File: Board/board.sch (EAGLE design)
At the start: 51 parts, among them IC1 L297, IC2 MEGA32-P, IC3 L298, J1 +12V, Q1 BC639, Q3 BC639, U2 DS1621+, X1 WATER_PUMP, X2 FAN, X5 SM_CD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

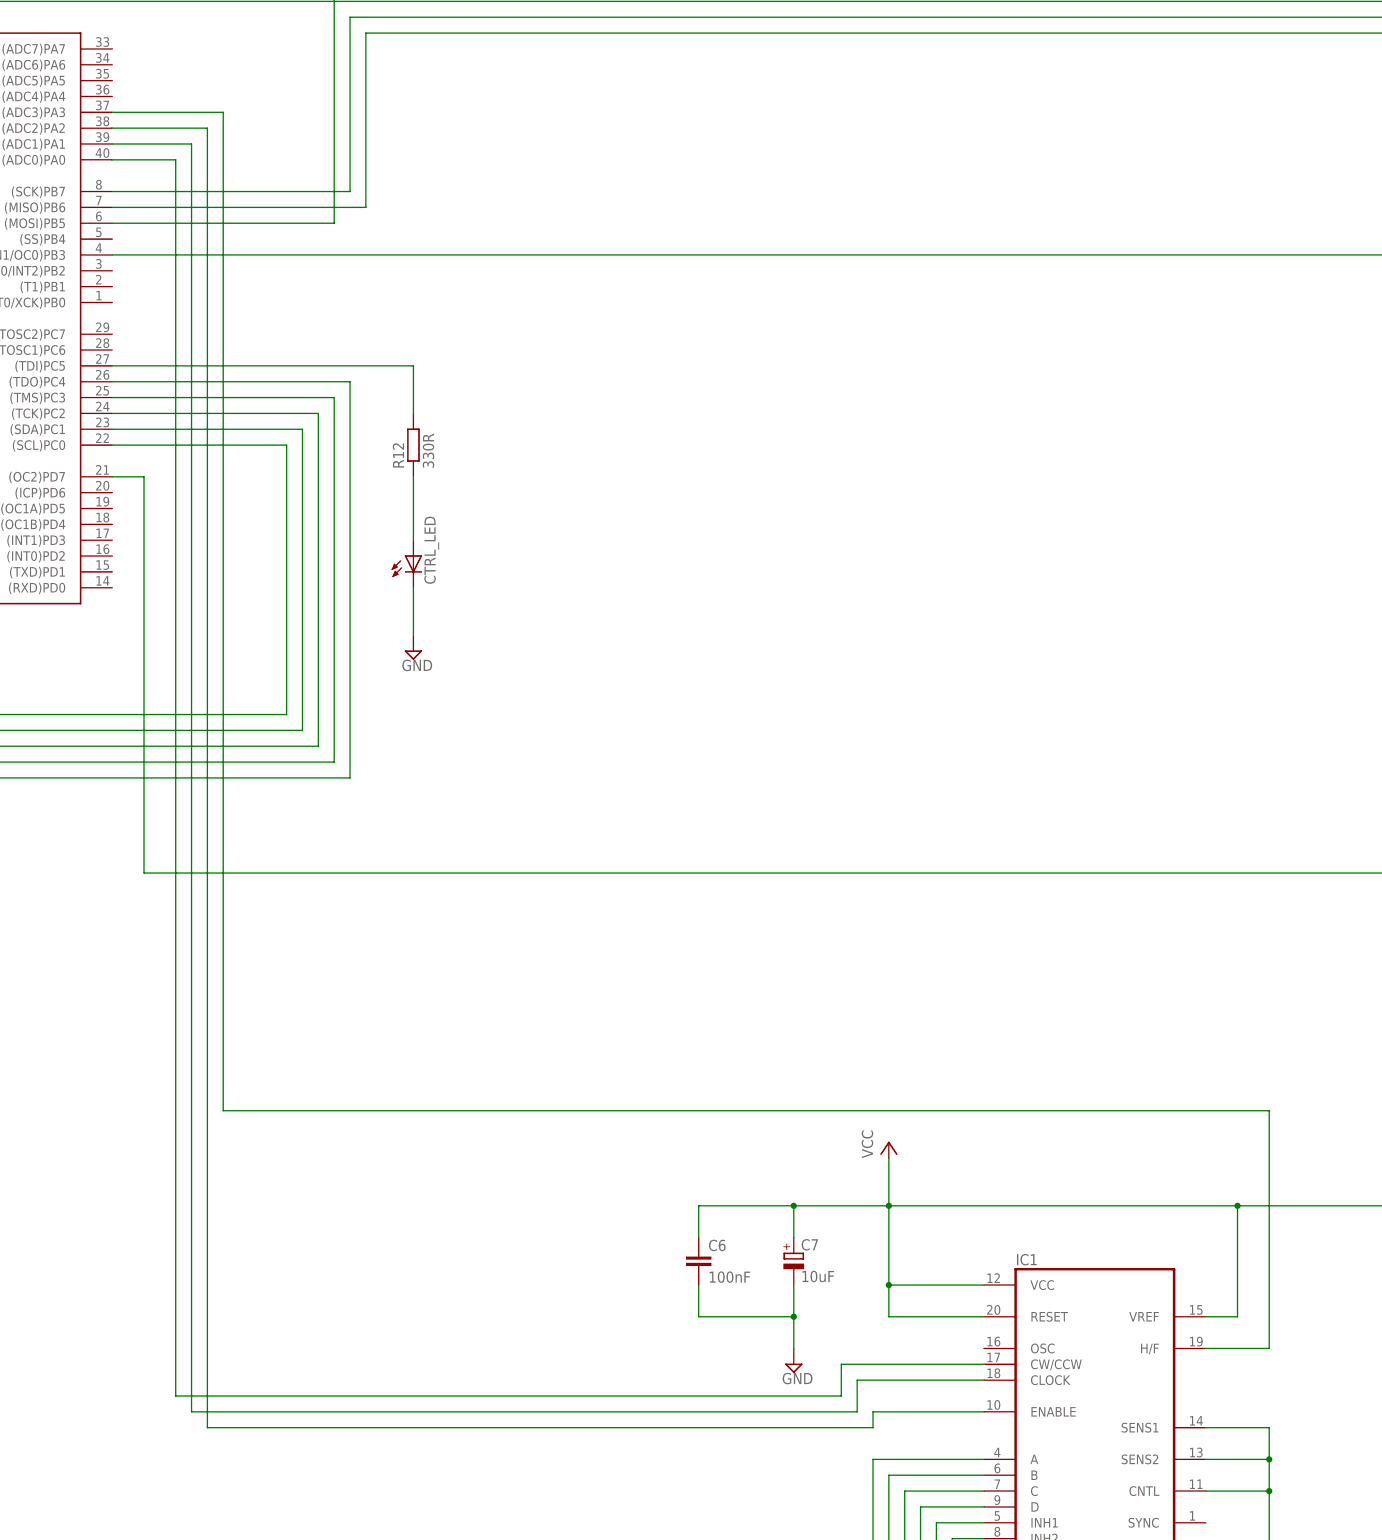
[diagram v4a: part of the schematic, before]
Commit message: PWM devices code
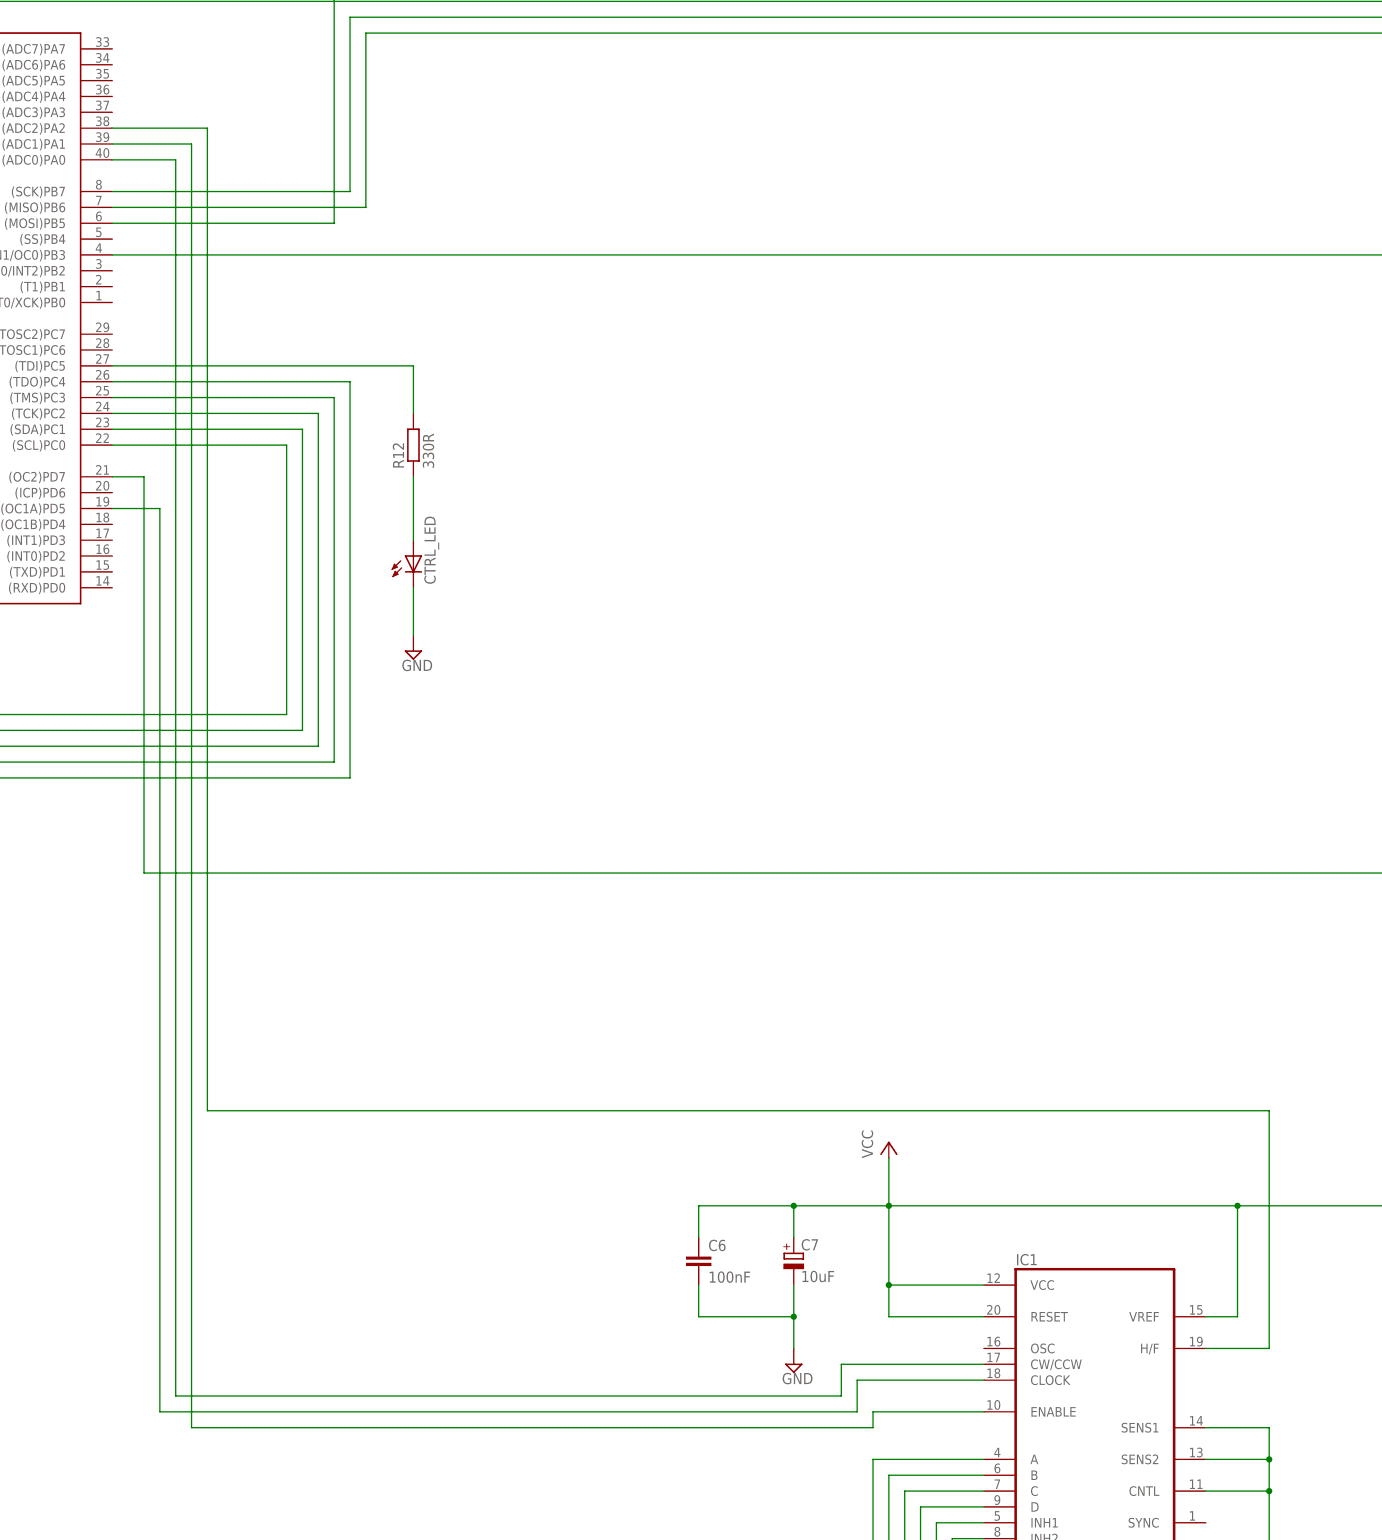
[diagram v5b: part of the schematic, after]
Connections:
- net N$18: now also IC2.(OC1A)PD5; no longer IC2.(ADC1)PA1
- net N$19: now also IC2.(ADC1)PA1; no longer IC2.(ADC2)PA2
- net N$20: now also IC2.(ADC2)PA2; no longer IC2.(ADC3)PA3
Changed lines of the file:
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@@
 <?xml version="1.0" encoding="utf-8"?>
 <!DOCTYPE eagle SYSTEM "eagle.dtd">
-<eagle version="7.6.0">
+<eagle version="8.7.1">
 <drawing>
 <settings>
 <setting alwaysvectorfont="no"/>
+<setting keepoldvectorfont="yes"/>
 <setting verticaltext="up"/>
 </settings>
@@
 <net name="N$18" class="0">
 <segment>
-<pinref part="IC2" gate="G$1" pin="(ADC1)PA1"/>
-<wire x1="-35.56" y1="38.1" x2="-22.86" y2="38.1" width="0.1524" layer="91"/>
-<wire x1="-22.86" y1="38.1" x2="-22.86" y2="-165.1" width="0.1524" layer="91"/>
-<wire x1="-22.86" y1="-165.1" x2="83.82" y2="-165.1" width="0.1524" layer="91"/>
+<wire x1="-27.94" y1="-165.1" x2="83.82" y2="-165.1" width="0.1524" layer="91"/>
 <pinref part="IC1" gate="L297" pin="CLOCK"/>
 <wire x1="104.14" y1="-160.02" x2="83.82" y2="-160.02" width="0.1524" layer="91"/>
 <wire x1="83.82" y1="-160.02" x2="83.82" y2="-165.1" width="0.1524" layer="91"/>
+<wire x1="-27.94" y1="-165.1" x2="-27.94" y2="-20.32" width="0.1524" layer="91"/>
+<pinref part="IC2" gate="G$1" pin="(OC1A)PD5"/>
+<wire x1="-27.94" y1="-20.32" x2="-35.56" y2="-20.32" width="0.1524" layer="91"/>
 </segment>
 </net>
 <net name="N$19" class="0">
 <segment>
-<pinref part="IC2" gate="G$1" pin="(ADC2)PA2"/>
-<wire x1="-35.56" y1="40.64" x2="-20.32" y2="40.64" width="0.1524" layer="91"/>
-<wire x1="-20.32" y1="40.64" x2="-20.32" y2="-167.64" width="0.1524" layer="91"/>
-<wire x1="-20.32" y1="-167.64" x2="86.36" y2="-167.64" width="0.1524" layer="91"/>
+<wire x1="-22.86" y1="-167.64" x2="86.36" y2="-167.64" width="0.1524" layer="91"/>
 <wire x1="86.36" y1="-167.64" x2="86.36" y2="-165.1" width="0.1524" layer="91"/>
 <pinref part="IC1" gate="L297" pin="ENABLE"/>
 <wire x1="86.36" y1="-165.1" x2="104.14" y2="-165.1" width="0.1524" layer="91"/>
+<pinref part="IC2" gate="G$1" pin="(ADC1)PA1"/>
+<wire x1="-22.86" y1="-167.64" x2="-22.86" y2="38.1" width="0.1524" layer="91"/>
+<wire x1="-22.86" y1="38.1" x2="-35.56" y2="38.1" width="0.1524" layer="91"/>
 </segment>
 </net>
@@
 <wire x1="139.7" y1="-154.94" x2="149.86" y2="-154.94" width="0.1524" layer="91"/>
 <wire x1="149.86" y1="-154.94" x2="149.86" y2="-116.84" width="0.1524" layer="91"/>
-<wire x1="149.86" y1="-116.84" x2="-17.78" y2="-116.84" width="0.1524" layer="91"/>
-<wire x1="-17.78" y1="-116.84" x2="-17.78" y2="43.18" width="0.1524" layer="91"/>
-<pinref part="IC2" gate="G$1" pin="(ADC3)PA3"/>
-<wire x1="-17.78" y1="43.18" x2="-35.56" y2="43.18" width="0.1524" layer="91"/>
-</segment>
-</net>
+<wire x1="149.86" y1="-116.84" x2="-20.32" y2="-116.84" width="0.1524" layer="91"/>
+<pinref part="IC2" gate="G$1" pin="(ADC2)PA2"/>
+<wire x1="-20.32" y1="-116.84" x2="-20.32" y2="40.64" width="0.1524" layer="91"/>
+<wire x1="-20.32" y1="40.64" x2="-35.56" y2="40.64" width="0.1524" layer="91"/>
+</segment>
+</net>

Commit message: Timr0 as counter, Timer1 output b for fan
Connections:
- removed net N$5: IC2.(AIN1/OC0)PB3, R1.1
- new net N$31: IC2.(OC1B)PD4, R1.1
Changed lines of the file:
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@@
 <?xml version="1.0" encoding="utf-8"?>
 <!DOCTYPE eagle SYSTEM "eagle.dtd">
-<eagle version="8.7.1">
+<eagle version="7.6.0">
 <drawing>
 <settings>
 <setting alwaysvectorfont="no"/>
-<setting keepoldvectorfont="yes"/>
 <setting verticaltext="up"/>
 </settings>
@@
 </segment>
 </net>
-<net name="N$5" class="0">
-<segment>
-<pinref part="IC2" gate="G$1" pin="(AIN1/OC0)PB3"/>
-<wire x1="-35.56" y1="20.32" x2="406.4" y2="20.32" width="0.1524" layer="91"/>
-<wire x1="406.4" y1="20.32" x2="406.4" y2="2.54" width="0.1524" layer="91"/>
-<pinref part="R1" gate="G$1" pin="1"/>
-<wire x1="406.4" y1="2.54" x2="416.56" y2="2.54" width="0.1524" layer="91"/>
-</segment>
-</net>
 <net name="N$9" class="0">
 <segment>
@@
 </segment>
 </net>
+<net name="N$31" class="0">
+<segment>
+<pinref part="R1" gate="G$1" pin="1"/>
+<wire x1="416.56" y1="2.54" x2="15.24" y2="2.54" width="0.1524" layer="91"/>
+<wire x1="15.24" y1="2.54" x2="15.24" y2="5.08" width="0.1524" layer="91"/>
+<wire x1="15.24" y1="5.08" x2="-17.78" y2="5.08" width="0.1524" layer="91"/>
+<pinref part="IC2" gate="G$1" pin="(OC1B)PD4"/>
+<wire x1="-17.78" y1="-22.86" x2="-35.56" y2="-22.86" width="0.1524" layer="91"/>
+<wire x1="-17.78" y1="5.08" x2="-17.78" y2="-22.86" width="0.1524" layer="91"/>
+</segment>
+</net>

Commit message: Added new inductor
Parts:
- L1: device inductors:DR127 -> inductors:BC12
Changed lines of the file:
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@@
 <part name="SUPPLY3" library="supply2" deviceset="GND" device=""/>
 <part name="D1" library="diode" deviceset="1N581*" device="" technology="9-B" value="1N5824"/>
-<part name="L1" library="inductors" deviceset="DR127" device="" value="33uH"/>
 <part name="C2" library="resistor" deviceset="CPOL-EU" device="E5-10.5" value="220uF"/>
 <part name="SUPPLY4" library="supply2" deviceset="GND" device=""/>
@@
 <part name="P+8" library="supply1" deviceset="VCC" device=""/>
 <part name="P+9" library="supply1" deviceset="VCC" device=""/>
+<part name="L1" library="inductors" deviceset="BC12" device="" value="33uH"/>
 </parts>
 <sheets>
@@
 <instance part="SUPPLY3" gate="GND" x="58.42" y="124.46"/>
 <instance part="D1" gate="G$1" x="81.28" y="134.62" rot="R90"/>
-<instance part="L1" gate="G$1" x="93.98" y="149.86"/>
 <instance part="C2" gate="G$1" x="106.68" y="137.16"/>
 <instance part="SUPPLY4" gate="GND" x="81.28" y="124.46"/>
@@
 <instance part="P+8" gate="VCC" x="-160.02" y="-60.96"/>
 <instance part="P+9" gate="VCC" x="-149.86" y="-60.96"/>
+<instance part="L1" gate="G$1" x="93.98" y="149.86"/>
 </instances>
 <busses>
@@
 <segment>
 <pinref part="LM2596" gate="G$1" pin="OUT"/>
-<pinref part="L1" gate="G$1" pin="1"/>
 <wire x1="68.58" y1="149.86" x2="81.28" y2="149.86" width="0.1524" layer="91"/>
 <pinref part="D1" gate="G$1" pin="C"/>
+<wire x1="81.28" y1="137.16" x2="81.28" y2="149.86" width="0.1524" layer="91"/>
+<pinref part="L1" gate="G$1" pin="1"/>
 <wire x1="81.28" y1="149.86" x2="86.36" y2="149.86" width="0.1524" layer="91"/>
-<wire x1="81.28" y1="137.16" x2="81.28" y2="149.86" width="0.1524" layer="91"/>
 <junction x="81.28" y="149.86"/>
 </segment>
@@
 <net name="VCC" class="0">
 <segment>
+<pinref part="C2" gate="G$1" pin="+"/>
+<pinref part="P+1" gate="VCC" pin="VCC"/>
+<wire x1="106.68" y1="144.78" x2="106.68" y2="139.7" width="0.1524" layer="91"/>
+<wire x1="106.68" y1="144.78" x2="106.68" y2="149.86" width="0.1524" layer="91"/>
+<pinref part="LM2596" gate="G$1" pin="FB"/>
+<wire x1="106.68" y1="149.86" x2="106.68" y2="162.56" width="0.1524" layer="91"/>
+<wire x1="68.58" y1="144.78" x2="106.68" y2="144.78" width="0.1524" layer="91"/>
+<junction x="106.68" y="144.78"/>
 <pinref part="L1" gate="G$1" pin="2"/>
 <wire x1="101.6" y1="149.86" x2="106.68" y2="149.86" width="0.1524" layer="91"/>
-<pinref part="C2" gate="G$1" pin="+"/>
-<wire x1="106.68" y1="149.86" x2="106.68" y2="144.78" width="0.1524" layer="91"/>
-<pinref part="P+1" gate="VCC" pin="VCC"/>
-<wire x1="106.68" y1="144.78" x2="106.68" y2="139.7" width="0.1524" layer="91"/>
-<wire x1="106.68" y1="149.86" x2="106.68" y2="162.56" width="0.1524" layer="91"/>
 <junction x="106.68" y="149.86"/>
-<pinref part="LM2596" gate="G$1" pin="FB"/>
-<wire x1="68.58" y1="144.78" x2="106.68" y2="144.78" width="0.1524" layer="91"/>
-<junction x="106.68" y="144.78"/>
-</segment>
-<segment>
+</segment>
+<segment>

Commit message: Resistor value
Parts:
- C1: value 680uF -> 470uF
- D1, D10, D3, D4, D5, D6, D7, D8, D9: value 1N5824 -> 1N5822
- R1, R5: value 220R -> 240R
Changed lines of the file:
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@@
 <part name="VSS1" library="supply1" deviceset="VSS" device=""/>
 <part name="F1" library="fuse" deviceset="FUSE" device="19560" value="250V/2A 135°C"/>
-<part name="C1" library="resistor" deviceset="CPOL-EU" device="E5-10.5" value="680uF"/>
+<part name="C1" library="resistor" deviceset="CPOL-EU" device="E5-10.5" value="470uF"/>
 <part name="SUPPLY1" library="supply2" deviceset="GND" device=""/>
 <part name="VSS2" library="supply1" deviceset="VSS" device=""/>
 <part name="SUPPLY2" library="supply2" deviceset="GND" device=""/>
 <part name="SUPPLY3" library="supply2" deviceset="GND" device=""/>
-<part name="D1" library="diode" deviceset="1N581*" device="" technology="9-B" value="1N5824"/>
+<part name="D1" library="diode" deviceset="1N581*" device="" technology="9-B" value="1N5822"/>
 <part name="C2" library="resistor" deviceset="CPOL-EU" device="E5-10.5" value="220uF"/>
 <part name="SUPPLY4" library="supply2" deviceset="GND" device=""/>
@@
 <part name="X2" library="con-ptr500" deviceset="AK500/3" device="" value="FAN"/>
 <part name="SUPPLY11" library="supply2" deviceset="GND" device=""/>
-<part name="R1" library="rcl" deviceset="R-EU_" device="0207/12" value="220R"/>
+<part name="R1" library="rcl" deviceset="R-EU_" device="0207/12" value="240R"/>
 <part name="VSS4" library="supply1" deviceset="VSS" device=""/>
 <part name="Q1" library="transistor-small-signal" deviceset="BC639" device=""/>
@@
 <part name="D2" library="diode" deviceset="1N581*" device="" technology="9-B" value="1N5824"/>
 <part name="SUPPLY20" library="supply2" deviceset="GND" device=""/>
-<part name="R5" library="rcl" deviceset="R-EU_" device="0207/12" value="220R"/>
+<part name="R5" library="rcl" deviceset="R-EU_" device="0207/12" value="240R"/>
 <part name="VSS6" library="supply1" deviceset="VSS" device=""/>
 <part name="Q3" library="transistor-small-signal" deviceset="BC639" device=""/>
 <part name="R7" library="rcl" deviceset="R-EU_" device="0207/12" value="470R"/>
 <part name="SUPPLY22" library="supply2" deviceset="GND" device=""/>
-<part name="D3" library="diode" deviceset="1N581*" device="" technology="9-B" value="1N5824"/>
-<part name="D4" library="diode" deviceset="1N581*" device="" technology="9-B" value="1N5824"/>
-<part name="D5" library="diode" deviceset="1N581*" device="" technology="9-B" value="1N5824"/>
-<part name="D6" library="diode" deviceset="1N581*" device="" technology="9-B" value="1N5824"/>
+<part name="D3" library="diode" deviceset="1N581*" device="" technology="9-B" value="1N5822"/>
+<part name="D4" library="diode" deviceset="1N581*" device="" technology="9-B" value="1N5822"/>
+<part name="D5" library="diode" deviceset="1N581*" device="" technology="9-B" value="1N5822"/>
+<part name="D6" library="diode" deviceset="1N581*" device="" technology="9-B" value="1N5822"/>
 <part name="SUPPLY13" library="supply2" deviceset="GND" device=""/>
 <part name="SUPPLY21" library="supply2" deviceset="GND" device=""/>
 <part name="SUPPLY23" library="supply2" deviceset="GND" device=""/>
 <part name="SUPPLY24" library="supply2" deviceset="GND" device=""/>
-<part name="D7" library="diode" deviceset="1N581*" device="" technology="9-B" value="1N5824"/>
-<part name="D8" library="diode" deviceset="1N581*" device="" technology="9-B" value="1N5824"/>
-<part name="D9" library="diode" deviceset="1N581*" device="" technology="9-B" value="1N5824"/>
-<part name="D10" library="diode" deviceset="1N581*" device="" technology="9-B" value="1N5824"/>
+<part name="D7" library="diode" deviceset="1N581*" device="" technology="9-B" value="1N5822"/>
+<part name="D8" library="diode" deviceset="1N581*" device="" technology="9-B" value="1N5822"/>
+<part name="D9" library="diode" deviceset="1N581*" device="" technology="9-B" value="1N5822"/>
+<part name="D10" library="diode" deviceset="1N581*" device="" technology="9-B" value="1N5822"/>
 <part name="SUPPLY28" library="supply2" deviceset="GND" device=""/>
 <part name="C9" library="rcl" deviceset="C-EU" device="025-025X050" value="100nF"/>
